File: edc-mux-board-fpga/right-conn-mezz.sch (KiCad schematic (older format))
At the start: 0 parts

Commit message: finished draft of horizontal pcb connector pinout.
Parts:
- added C? (x12): 1uF, Capacitor_SMD:C_0805_2012Metric, symbol Device:C_Small
- added D? (x30): 30pF 30kV, Diode_SMD:D_0402_1005Metric, symbol Device:D_TVS
- added D? (x6): 12V_Vrso, Diode_SMD:D_SMA, symbol Device:D_TVS
- added F? (x6): 1A, Fuse:Fuse_0603_1608Metric, symbol Device:Polyfuse_Small
- added FB? (x24): 600Ω @ 100MHz, Capacitor_SMD:C_0805_2012Metric, symbol Device:Ferrite_Bead_Small
- added J?: Device 10, Connector_PinHeader_1.27mm:PinHeader_2x06_P1.27mm_Vertical, symbol Connector_Generic:Conn_01x12
- added J?: Left Mezzanine Board Connector (Daughterboard), symbol Connector_Generic:Conn_02x40_Odd_Even
- added J?: Device 11, Connector_PinHeader_1.27mm:PinHeader_2x06_P1.27mm_Vertical, symbol Connector_Generic:Conn_01x12
- added J?: Device 12, Connector_PinHeader_1.27mm:PinHeader_2x06_P1.27mm_Vertical, symbol Connector_Generic:Conn_01x12
- added J?: Device 13, Connector_PinHeader_1.27mm:PinHeader_2x06_P1.27mm_Vertical, symbol Connector_Generic:Conn_01x12
- added J?: Device 14, Connector_PinHeader_1.27mm:PinHeader_2x06_P1.27mm_Vertical, symbol Connector_Generic:Conn_01x12
- added J?: Device 15, Connector_PinHeader_1.27mm:PinHeader_2x06_P1.27mm_Vertical, symbol Connector_Generic:Conn_01x12
- added J?: Left Mezzanine Board Connector (Motherboard), symbol Connector_Generic:Conn_02x40_Odd_Even
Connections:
- new net: D?.1 (A1), F?.2, J?.12 (Pin_12) (x6)
- new net: D?.1 (A1), FB?.2, J?.2 (Pin_2) (x6)
- new net: D?.1 (A1), FB?.2, J?.3 (Pin_3) (x6)
- new net: D?.1 (A1), FB?.2, J?.4 (Pin_4) (x6)
- new net: D?.1 (A1), FB?.2, J?.5 (Pin_5) (x6)
- new net: C?.2, FB?.1 (x12)
- new net +12V: J?.37 (Pin_37), J?.38 (Pin_38), J?.39 (Pin_39), J?.40 (Pin_40), J?.41 (Pin_41), J?.42 (Pin_42), J?.43 (Pin_43), J?.44 (Pin_44)
- new net AUD_GND10: J?.5 (Pin_5)
- new net AUD_GND11: J?.17 (Pin_17)
- new net AUD_GND12: J?.29 (Pin_29)
- new net AUD_GND13: J?.51 (Pin_51)
- new net AUD_GND14: J?.63 (Pin_63)
- new net AUD_GND15: J?.75 (Pin_75)
- new net GND: J?.11 (Pin_11), J?.12 (Pin_12), J?.18 (Pin_18), J?.23 (Pin_23), J?.24 (Pin_24), J?.30 (Pin_30), J?.35 (Pin_35), J?.36 (Pin_36), J?.45 (Pin_45), J?.46 (Pin_46), J?.52 (Pin_52), J?.57 (Pin_57), J?.58 (Pin_58), J?.6 (Pin_6), J?.64 (Pin_64), J?.69 (Pin_69), J?.70 (Pin_70), J?.76 (Pin_76)
- new net ID_PIN10: J?.9 (Pin_9)
- new net ID_PIN11: J?.21 (Pin_21)
- new net ID_PIN12: J?.33 (Pin_33)
- new net ID_PIN13: J?.55 (Pin_55)
- new net ID_PIN14: J?.67 (Pin_67)
- new net ID_PIN15: J?.79 (Pin_79)
- new net INT_10: J?.7 (Pin_7)
- new net INT_11: J?.19 (Pin_19)
- new net INT_12: J?.31 (Pin_31)
- new net INT_13: J?.53 (Pin_53)
- new net INT_14: J?.65 (Pin_65)
- new net INT_15: J?.77 (Pin_77)
- new net L_IN10: J?.3 (Pin_3)
- new net L_IN11: J?.15 (Pin_15)
- new net L_IN12: J?.27 (Pin_27)
- new net L_IN13: J?.49 (Pin_49)
- new net L_IN14: J?.61 (Pin_61)
- new net L_IN15: J?.73 (Pin_73)
- new net L_OUT10: J?.4 (Pin_4)
- new net L_OUT11: J?.16 (Pin_16)
- new net L_OUT12: J?.28 (Pin_28)
- new net L_OUT13: J?.50 (Pin_50)
- new net L_OUT14: J?.62 (Pin_62)
- new net L_OUT15: J?.74 (Pin_74)
- new net M_+12V: F?.1, F?.1, F?.1, F?.1, F?.1, F?.1, J?.37 (Pin_37), J?.38 (Pin_38), J?.39 (Pin_39), J?.40 (Pin_40), J?.41 (Pin_41), J?.42 (Pin_42), J?.43 (Pin_43), J?.44 (Pin_44)
- new net M_AUD_GND10: J?.1 (Pin_1), J?.5 (Pin_5)
- new net M_AUD_GND11: J?.1 (Pin_1), J?.17 (Pin_17)
- new net M_AUD_GND12: J?.1 (Pin_1), J?.29 (Pin_29)
- new net M_AUD_GND13: J?.1 (Pin_1), J?.51 (Pin_51)
- new net M_AUD_GND14: J?.1 (Pin_1), J?.63 (Pin_63)
- new net M_AUD_GND15: J?.1 (Pin_1), J?.75 (Pin_75)
- new net M_GND: D?.2 (A2), D?.2 (A2), D?.2 (A2), D?.2 (A2), D?.2 (A2), D?.2 (A2), D?.2 (A2), D?.2 (A2), D?.2 (A2), D?.2 (A2), D?.2 (A2), D?.2 (A2), D?.2 (A2), D?.2 (A2), D?.2 (A2), D?.2 (A2), D?.2 (A2), D?.2 (A2), D?.2 (A2), D?.2 (A2), D?.2 (A2), D?.2 (A2), D?.2 (A2), D?.2 (A2), D?.2 (A2), D?.2 (A2), D?.2 (A2), D?.2 (A2), D?.2 (A2), D?.2 (A2), D?.2 (A2), D?.2 (A2), D?.2 (A2), D?.2 (A2), D?.2 (A2), D?.2 (A2), J?.10 (Pin_10), J?.10 (Pin_10), J?.10 (Pin_10), J?.10 (Pin_10), J?.10 (Pin_10), J?.10 (Pin_10), J?.10 (Pin_10), J?.11 (Pin_11), J?.12 (Pin_12), J?.18 (Pin_18), J?.23 (Pin_23), J?.24 (Pin_24), J?.30 (Pin_30), J?.35 (Pin_35), J?.36 (Pin_36), J?.45 (Pin_45), J?.46 (Pin_46), J?.52 (Pin_52), J?.57 (Pin_57), J?.58 (Pin_58), J?.6 (Pin_6), J?.6 (Pin_6), J?.6 (Pin_6), J?.6 (Pin_6), J?.6 (Pin_6), J?.6 (Pin_6), J?.6 (Pin_6), J?.64 (Pin_64), J?.69 (Pin_69), J?.7 (Pin_7), J?.7 (Pin_7), J?.70 (Pin_70), J?.76 (Pin_76), J?.8 (Pin_8), J?.8 (Pin_8), J?.9 (Pin_9)
- new net M_ID_PIN10: D?.1 (A1), J?.11 (Pin_11), J?.9 (Pin_9)
- new net M_ID_PIN11: D?.1 (A1), J?.11 (Pin_11), J?.21 (Pin_21)
- new net M_ID_PIN12: D?.1 (A1), J?.11 (Pin_11), J?.33 (Pin_33)
- new net M_ID_PIN13: D?.1 (A1), J?.11 (Pin_11), J?.55 (Pin_55)
- new net M_ID_PIN14: D?.1 (A1), J?.11 (Pin_11), J?.67 (Pin_67)
- new net M_ID_PIN15: D?.1 (A1), J?.11 (Pin_11), J?.79 (Pin_79)
- new net M_INT_11: J?.19 (Pin_19), J?.9 (Pin_9)
- new net M_INT_12: J?.31 (Pin_31), J?.9 (Pin_9)
- new net M_INT_13: J?.53 (Pin_53), J?.9 (Pin_9)
- new net M_INT_14: J?.65 (Pin_65), J?.9 (Pin_9)
- new net M_INT_15: J?.77 (Pin_77), J?.9 (Pin_9)
- new net M_L_IN10: C?.1, J?.3 (Pin_3)
- new net M_L_IN11: C?.1, J?.15 (Pin_15)
- new net M_L_IN12: C?.1, J?.27 (Pin_27)
- new net M_L_IN13: C?.1, J?.49 (Pin_49)
- new net M_L_IN14: C?.1, J?.61 (Pin_61)
- new net M_L_IN15: C?.1, J?.73 (Pin_73)
- new net M_L_OUT10: FB?.1, J?.2 (Pin_2)
- new net M_L_OUT11: FB?.1, J?.16 (Pin_16)
- new net M_L_OUT12: FB?.1, J?.28 (Pin_28)
- new net M_L_OUT13: FB?.1, J?.50 (Pin_50)
- new net M_L_OUT14: FB?.1, J?.62 (Pin_62)
- new net M_L_OUT15: FB?.1, J?.74 (Pin_74)
- new net M_R_IN10: C?.1, J?.1 (Pin_1)
- new net M_R_IN11: C?.1, J?.13 (Pin_13)
- new net M_R_IN12: C?.1, J?.25 (Pin_25)
- new net M_R_IN13: C?.1, J?.47 (Pin_47)
- new net M_R_IN14: C?.1, J?.59 (Pin_59)
- new net M_R_IN15: C?.1, J?.71 (Pin_71)
- new net M_R_OUT10: FB?.1, J?.4 (Pin_4)
- new net M_R_OUT11: FB?.1, J?.14 (Pin_14)
- new net M_R_OUT12: FB?.1, J?.26 (Pin_26)
- new net M_R_OUT13: FB?.1, J?.48 (Pin_48)
- new net M_R_OUT14: FB?.1, J?.60 (Pin_60)
- new net M_R_OUT15: FB?.1, J?.72 (Pin_72)
- new net M_SCL_HV11: J?.20 (Pin_20), J?.8 (Pin_8)
- new net M_SCL_HV12: J?.32 (Pin_32), J?.8 (Pin_8)
- new net M_SCL_HV13: J?.54 (Pin_54), J?.8 (Pin_8)
- new net M_SCL_HV14: J?.66 (Pin_66), J?.8 (Pin_8)
- new net M_SCL_HV15: J?.78 (Pin_78), J?.8 (Pin_8)
- new net M_SDA_HV11: J?.22 (Pin_22), J?.7 (Pin_7)
- new net M_SDA_HV12: J?.34 (Pin_34), J?.7 (Pin_7)
- new net M_SDA_HV13: J?.56 (Pin_56), J?.7 (Pin_7)
- new net M_SDA_HV14: J?.68 (Pin_68), J?.7 (Pin_7)
- new net M_SDA_HV15: J?.7 (Pin_7), J?.80 (Pin_80)
- new net R_IN10: J?.1 (Pin_1)
- new net R_IN11: J?.13 (Pin_13)
- new net R_IN12: J?.25 (Pin_25)
- new net R_IN13: J?.47 (Pin_47)
- new net R_IN14: J?.59 (Pin_59)
- new net R_IN15: J?.71 (Pin_71)
- new net R_OUT10: J?.2 (Pin_2)
- new net R_OUT11: J?.14 (Pin_14)
- new net R_OUT12: J?.26 (Pin_26)
- new net R_OUT13: J?.48 (Pin_48)
- new net R_OUT14: J?.60 (Pin_60)
- new net R_OUT15: J?.72 (Pin_72)
- new net SCL_HV10: J?.8 (Pin_8)
- new net SCL_HV11: J?.20 (Pin_20)
- new net SCL_HV12: J?.32 (Pin_32)
- new net SCL_HV13: J?.54 (Pin_54)
- new net SCL_HV14: J?.66 (Pin_66)
- new net SCL_HV15: J?.78 (Pin_78)
- new net SDA_HV10: J?.10 (Pin_10)
- new net SDA_HV11: J?.22 (Pin_22)
- new net SDA_HV12: J?.34 (Pin_34)
- new net SDA_HV13: J?.56 (Pin_56)
- new net SDA_HV14: J?.68 (Pin_68)
- new net SDA_HV15: J?.80 (Pin_80)
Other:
- note added: "DC Blocking Caps\nDue to high input resistance\n(see datasheet)\nthese caps can be much \nsmaller than normal"
- note added: "Place film caps and\nferrite beads close\nto connector"

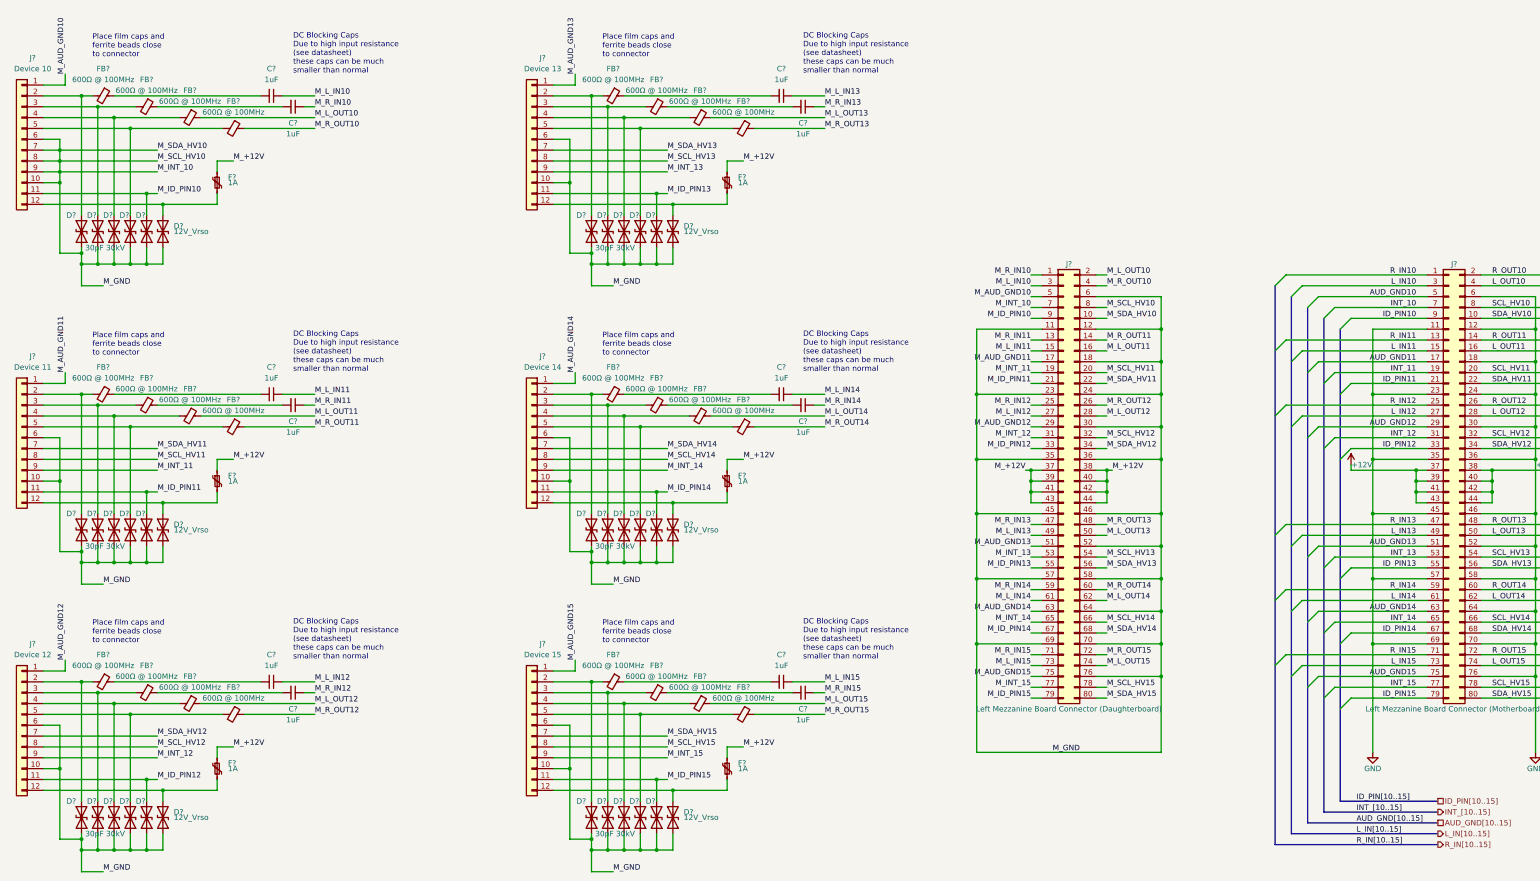
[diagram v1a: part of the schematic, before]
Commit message: Finished FPGA and MCU interconnections.
Finished up interrupt wiring
Fixed a few missing connections
Annotated Schematic
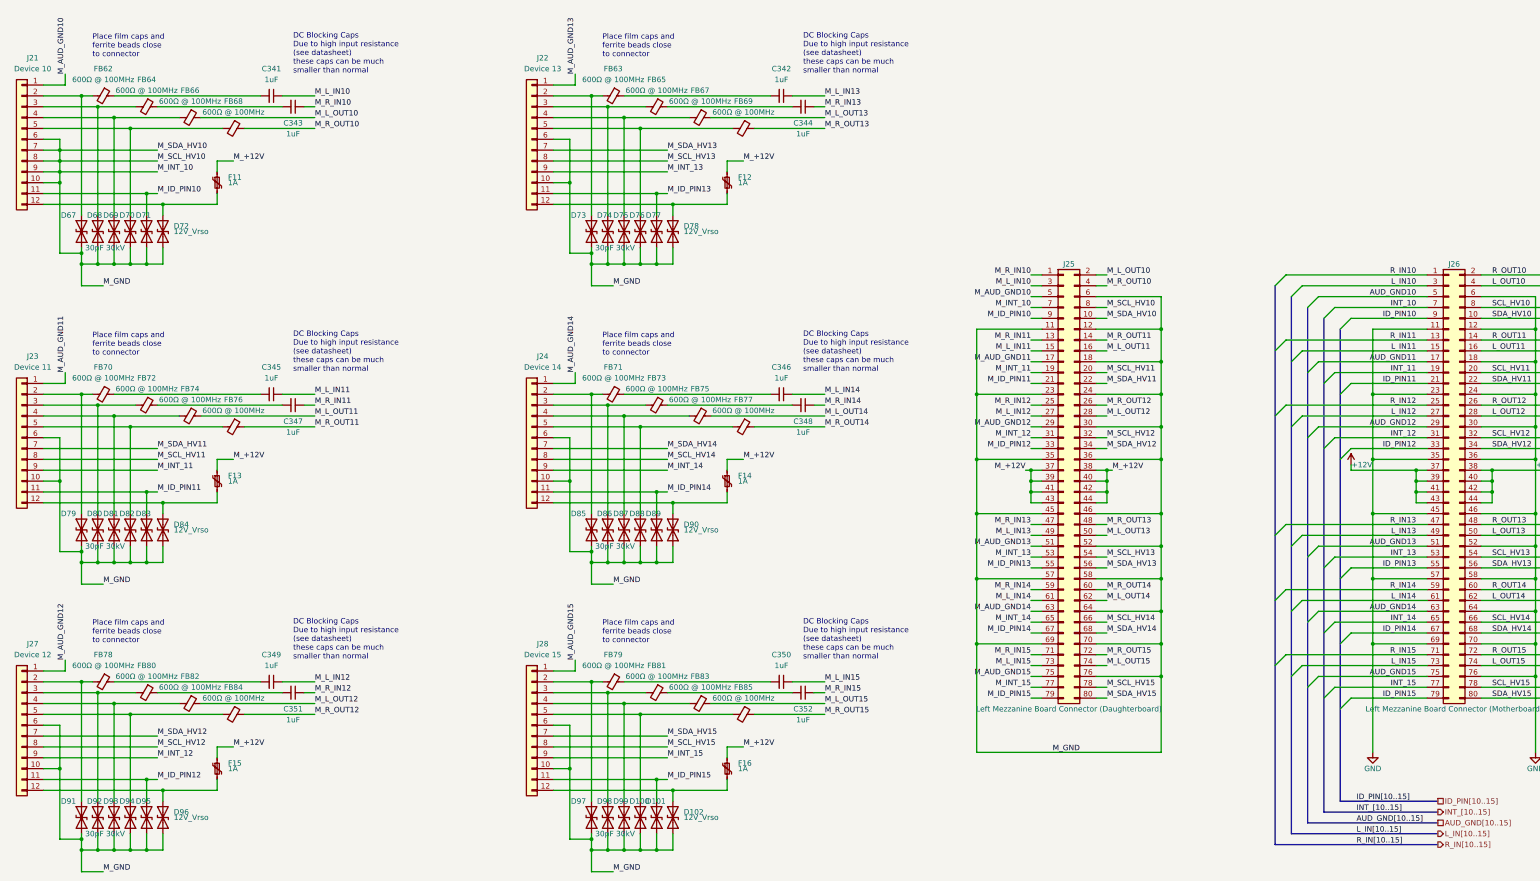
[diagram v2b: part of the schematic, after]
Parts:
- gave numbers to parts that had none: 86
